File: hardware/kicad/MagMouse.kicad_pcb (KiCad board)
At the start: 4 copper layers, 50 x 95 mm, 316 parts, among them J1 TYPE-C-31-M-12, J2 COIL_L, J3 COIL_M, J4 COIL_R, J5 GB1806 phase wires, Q1 2N7002, Q2 2N7002, Q3 2N7002, Q4 2N7002, Q5 AO3400A, SW1 RESET, SW2 BOOT, U1 TPD2EUSB30DRTR, U10 ADS7038IRTER, U11 TUSB320LAIRWBR, U12 TPS259470LRPWR, U13 TPS259470LRPWR, U14 SN74LVC2G04DCKR, U15 SN74LVC1G123DCUR, U16 SN74LVC08APWR, U17 SN74LVC08APWR, U18 SN74LVC08APWR, U19 TLV9001IDBVR, U2 TPS62162DSGR, U20 TPD2E2U06DCKR, U21 DRV8316RRGFR, U22 SN74LVC08APWR, U23 ADS7038IRTER, U24 SN74LVC125APWR, U25 SN74LVC125APWR, U26 SN74LVC125APWR, U27 MA735GGU-P, U28 TPS22919DCKR, U29 SN74LVC125APWR, U3 ESP32-S3-MINI-1-N8, U30 TLV1811DBVR, U31 LM4040AIM3-2.5/NOPB, U32 ICM-42688-P, U33 TPS7A2450DBVR, U34 SN74LV1T34DBVR, U35 PMW3360DM-T2QU, U36 TLV75519PDBVR, U37 SN74LVC125APWR, U38 TPS22918DBVR, U39 SN74LVC1G125DBVR, U4 DRV8231ADSGR, U5 DRV8231ADSGR, U6 DRV8231ADSGR, U7 TMAG5253BA2IQDMRR, U8 TMAG5253BA2IQDMRR, U9 TMAG5253BA2IQDMRR

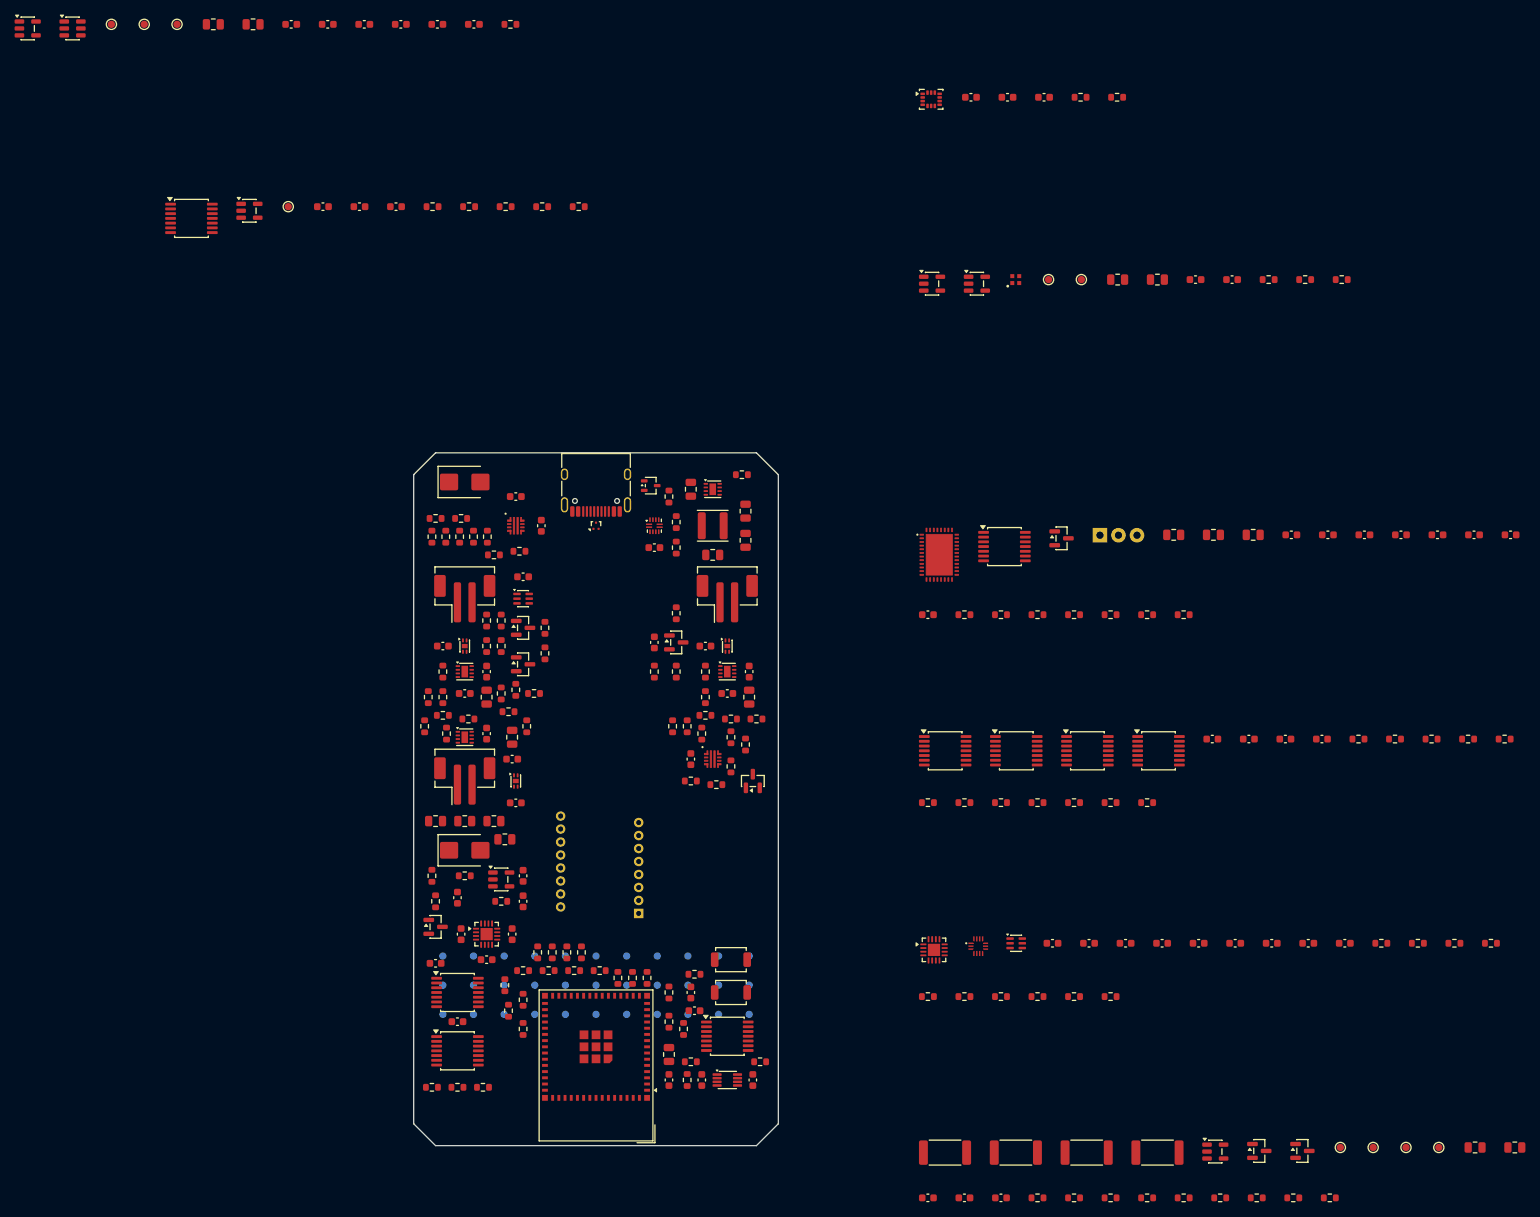
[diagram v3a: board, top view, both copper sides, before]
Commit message: Place motherboard, add upright encoder PCB and route logic buck
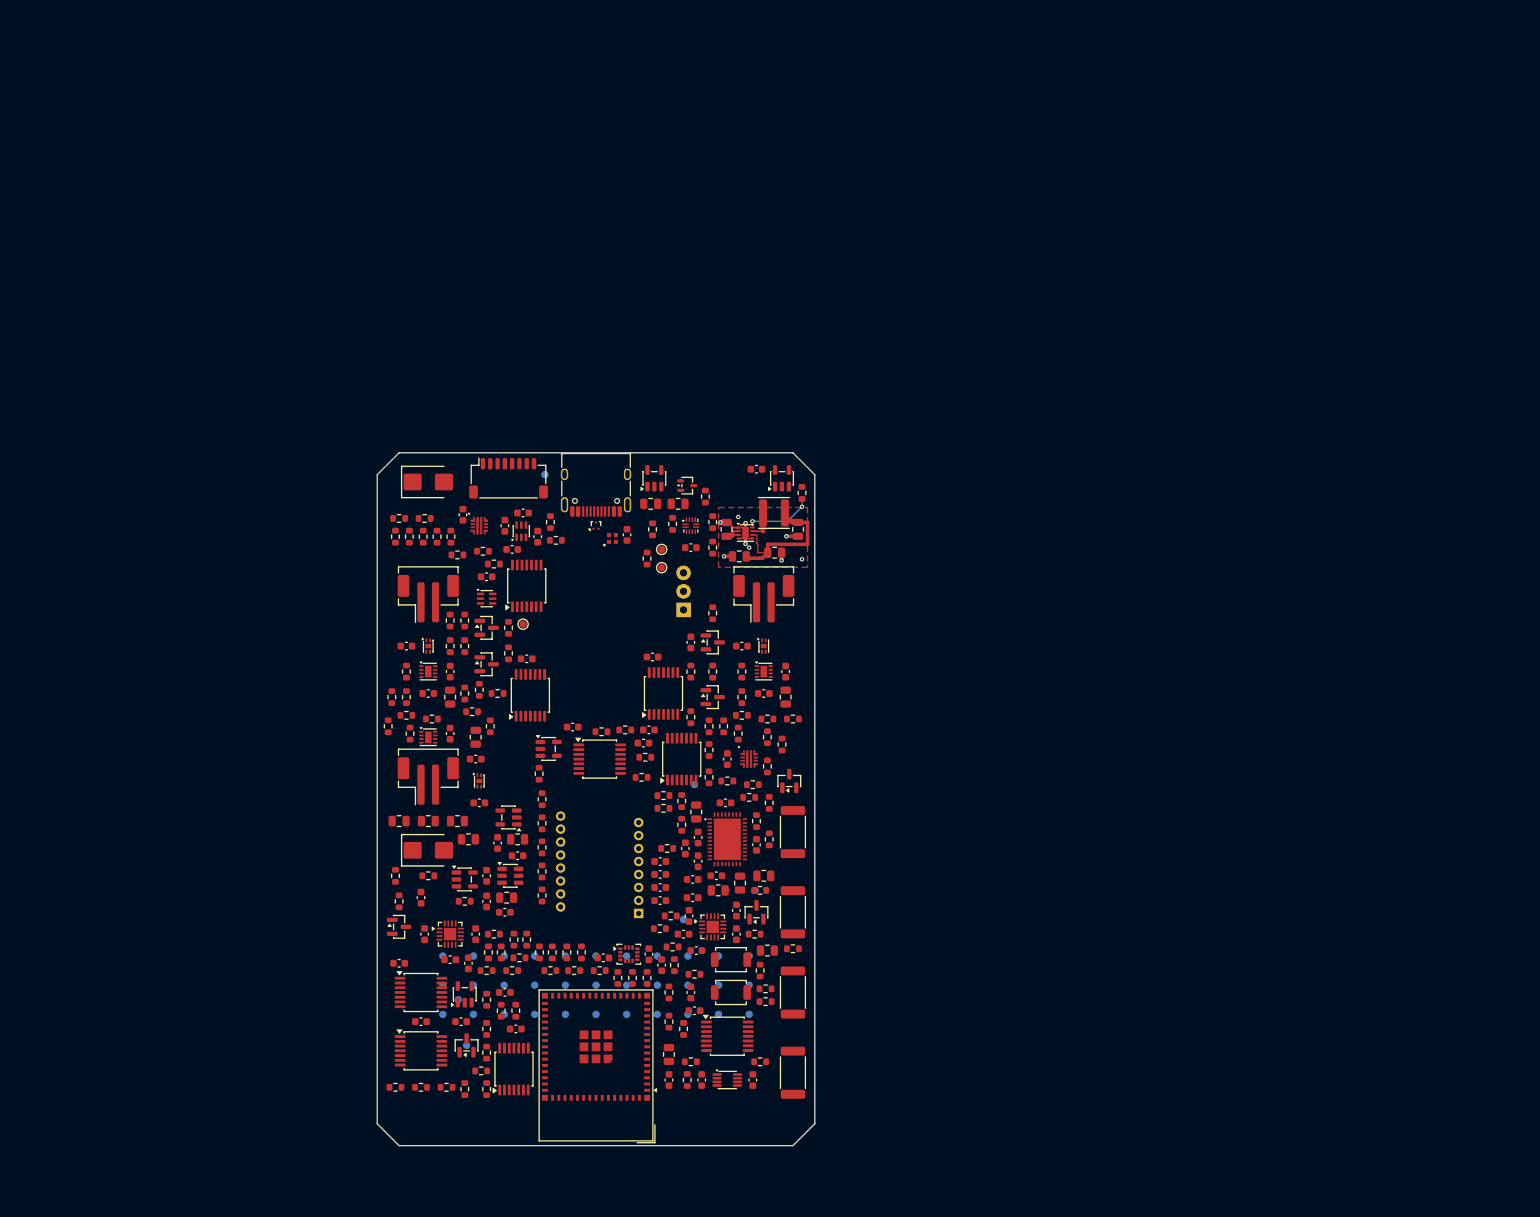
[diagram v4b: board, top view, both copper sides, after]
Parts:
- removed C62: 1uF/50V, Capacitor_SMD:C_0603_1608Metric
- removed U27: MA735GGU-P, MagMouse:MPS_UTQFN14_2x2
- added J6: ENCODER_8P, Connector_JST:JST_SH_SM08B-SRSS-TB_1x08-1MP_P1.00mm_Horizontal, F.Cu at (113.0, 103.5)
- TP34, TP35, TP36, TP40, TP41, TP42, TP43: moved to B.Cu
- moved TP40 148.0 mm to (146.8, 160.0), turned to 180 degrees
- moved TP37 144.6 mm to (115.0, 123.5)
- moved TP41 143.0 mm to (142.8, 160.0), turned to 180 degrees
- moved TP34 142.8 mm to (118.0, 103.0), turned to 180 degrees
- moved R127 142.7 mm to (118.8, 171.0)
- moved TP42 141.0 mm to (137.0, 164.0), turned to 180 degrees
- moved C72 132.6 mm to (126.0, 169.2)
- moved TP36 131.5 mm to (106.1, 175.0)
- moved R126 131.4 mm to (135.8, 170.2), turned to 90 degrees
- moved U38 130.8 mm to (113.2, 158.0)
- moved C71 128.1 mm to (134.0, 170.2), turned to 90 degrees
- moved C64 127.2 mm to (115.0, 108.2)
- moved U36 126.7 mm to (113.0, 150.0), turned to 180 degrees
- moved C77 126.3 mm to (112.8, 161.0)
- moved C70 125.5 mm to (132.2, 168.8), turned to 90 degrees
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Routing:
- net +3V3: track 0.00 -> 21.5 mm
- net GND: track 0.00 -> 10.7 mm, vias 0 -> 9
- net LOGIC_PG: track 0.00 -> 9.55 mm, vias 0 -> 2
- net BUCK_SW: track 0.00 -> 3.95 mm
- net PWR_5V: track 0.00 -> 3.65 mm
- added copper zone on F.Cu, net GND
- added copper zone on In1.Cu, net GND
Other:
- board size 50 x 95 mm -> 60 x 95 mm
- board text added: "60 x 95 mm - PROVISIONAL OUTLINE"
- board text added: "J6 -> ENCODER J7 / PIN N TO PIN N VERIFY PLUG + WIRE CLEARANCE ABOVE FRONT PARTS"
- board text added: "WHEEL + UPRIGHT ENCODER - PROVISIONAL"
- board text removed: "50 x 95 mm - PROVISIONAL OUTLINE"
- board text removed: "IMU"
- board text removed: "RGB"
- board text removed: "STAGED 10 Wheel Driver - NOT PLACED"
- board text removed: "STAGED 11 Wheel SPI - NOT PLACED"
- board text removed: "STAGED 12 Wheel Feedback - NOT PLACED"
- board text removed: "STAGED 13 Regeneration Brake - NOT PLACED"
- board text removed: "STAGED 14 IMU - NOT PLACED"
- board text removed: "STAGED 15 RGB Status - NOT PLACED"
- board text removed: "STAGED 16 Optical Power - NOT PLACED"
- board text removed: "STAGED 17 Optical Support - U35 ON BOARD"
- board text removed: "WHEEL DRIVE / ADC2 BRAKE RESERVE"
- board text removed: "WHEEL MECHANICS PROVISIONAL"

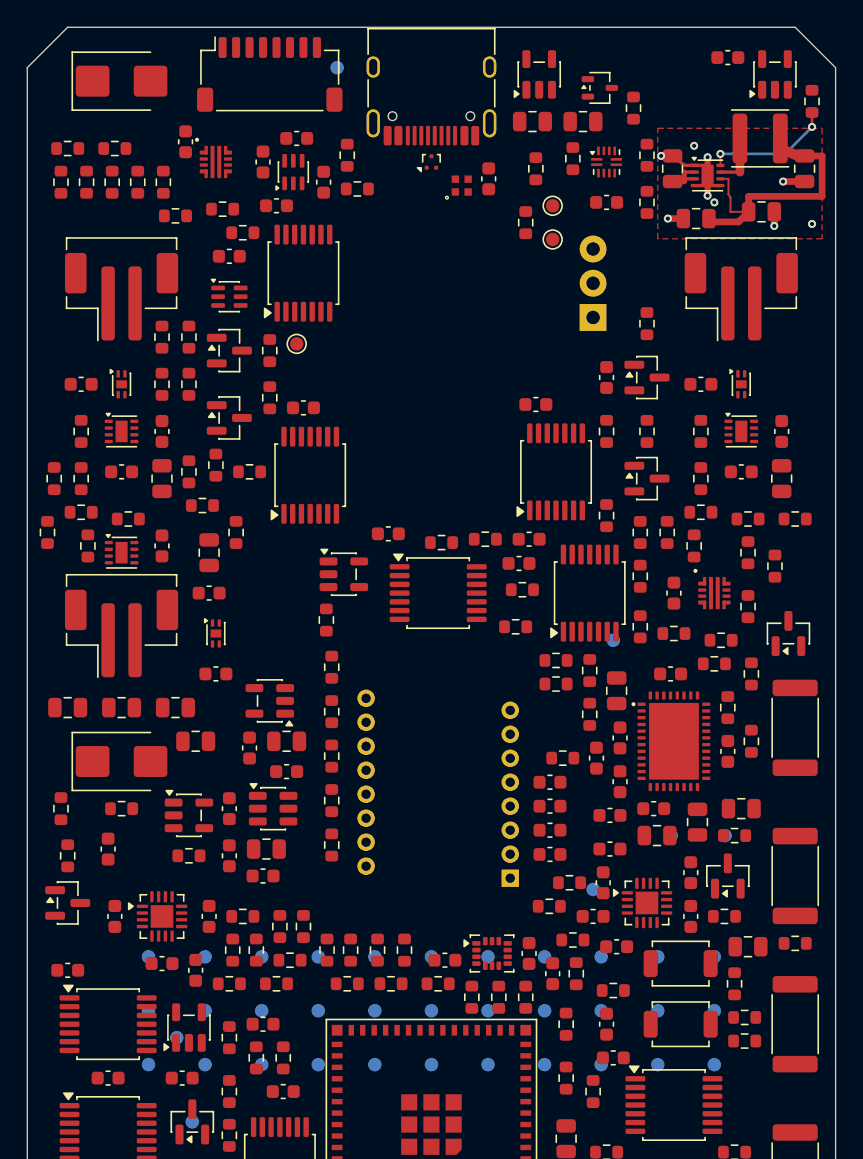
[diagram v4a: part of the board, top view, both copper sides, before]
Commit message: Route input power and Type-C detection, select PCB stackup
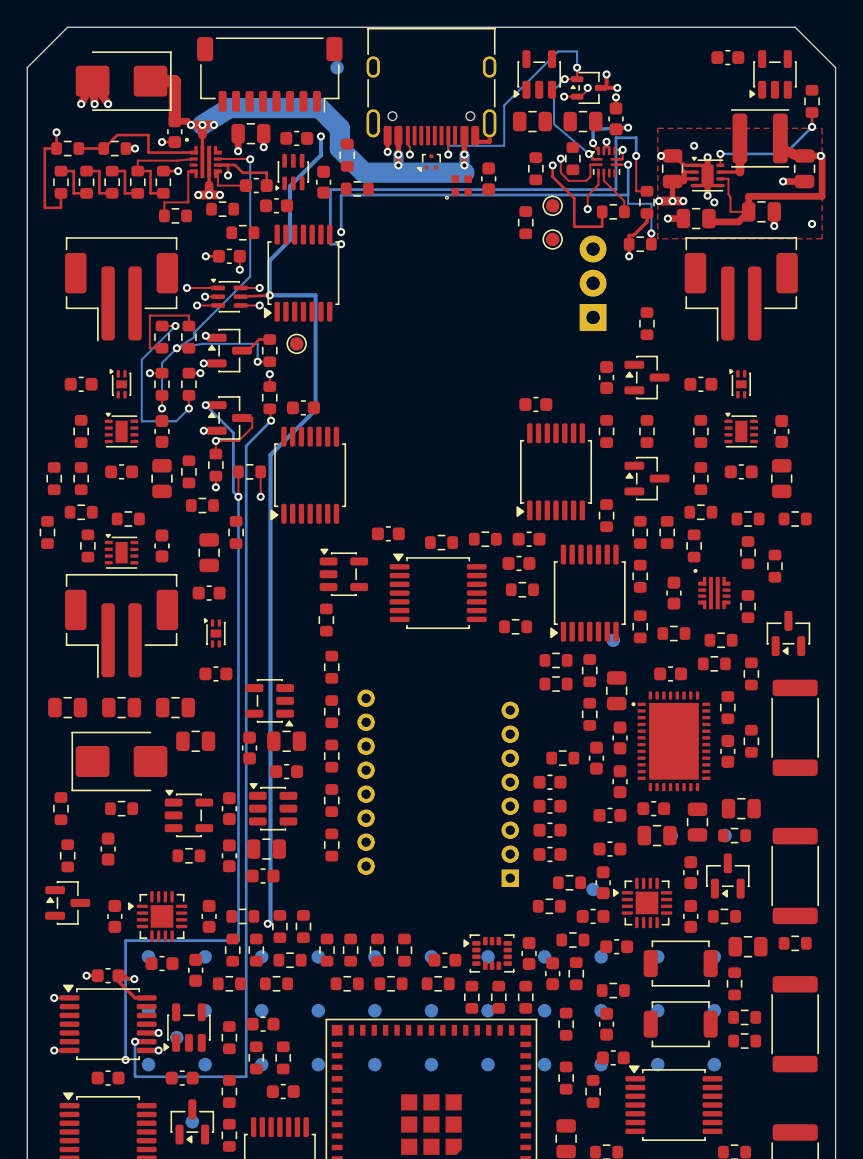
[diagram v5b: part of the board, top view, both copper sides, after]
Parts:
- added C88: 10uF/25V, Capacitor_SMD:C_0805_2012Metric, F.Cu at (111.6, 107.9)
- moved R25 7.84 mm to (138.5, 113.7), turned to 0 degrees
- moved R26 6.62 mm to (140.5, 116.1), turned to 0 degrees
- moved C22 6.24 mm to (138.7, 106.8), turned to 90 degrees
- moved C29 3.03 mm to (101.0, 170.4), turned to 180 degrees
- moved C25 1.82 mm to (112.0, 111.8), turned to 0 degrees
- moved C24 1.10 mm to (106.0, 107.8), turned to -90 degrees
- moved U20 0.80 mm to (136.7, 104.5)
- moved U12 0.75 mm to (108.2, 110.0)
- turned D1 to 180 degrees
- turned J6 to 180 degrees
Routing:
- net +3V3: track 21.5 -> 211.4 mm, vias 0 -> 9
- net SOURCE_OK: track 0.00 -> 90.1 mm, vias 0 -> 5
- net VBUS_USB: track 0.00 -> 73.9 mm, vias 0 -> 9
- net SOURCE_3A: track 0.00 -> 64.7 mm, vias 0 -> 4
- net CC_OUT2_INV: track 0.00 -> 61.5 mm, vias 0 -> 2
- net CC_OUT2: track 0.00 -> 55.4 mm, vias 0 -> 4
- net USB_ILM: track 0.00 -> 54.1 mm, vias 0 -> 5
- net PWR_5V: track 3.65 -> 54.8 mm, vias 0 -> 7
- net CC_OUT1: track 0.00 -> 50.5 mm, vias 0 -> 4
- net GND: track 10.7 -> 47.4 mm, vias 9 -> 32
- net USB_CC2: track 0.00 -> 29.0 mm, vias 0 -> 4
- net USB_CC1: track 0.00 -> 27.1 mm, vias 0 -> 4
- net ILM_HIGH_D: track 0.00 -> 15.1 mm, vias 0 -> 2
- net ILM_BASE_2: track 0.00 -> 14.0 mm, vias 0 -> 2
- net USB_UVLO: track 0.00 -> 10.2 mm
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
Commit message: Route U13 local actuator power and protection
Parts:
- added C89: 1uF/50V, Capacitor_SMD:C_0603_1608Metric, F.Cu at (146.0, 139.0)
- moved C40 38.6 mm to (145.2, 144.9)
- moved R42 10.6 mm to (151.0, 138.1)
- moved C26 6.39 mm to (148.5, 145.2), turned to 0 degrees
- moved R43 5.46 mm to (151.0, 142.4)
- moved R40 3.16 mm to (153.5, 139.0)
- moved D3 0.32 mm to (151.8, 145.1)
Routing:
- net PWR_5V: track 54.8 -> 104.3 mm, vias 7 -> 12
- net ACT_UVLO: track 0.00 -> 30.3 mm, vias 0 -> 3
- net ACT_OVLO: track 0.00 -> 19.6 mm, vias 0 -> 3
- net ACT_ILM: track 0.00 -> 9.05 mm
- net GND: track 47.4 -> 54.6 mm, vias 32 -> 39
- net ACT_5V: track 0.00 -> 6.95 mm, vias 0 -> 3
- net ACT_UV_2: track 0.00 -> 4.65 mm
- net ACT_UV_1: track 0.00 -> 3.65 mm
- net ACT_DVDT: track 0.00 -> 3.02 mm

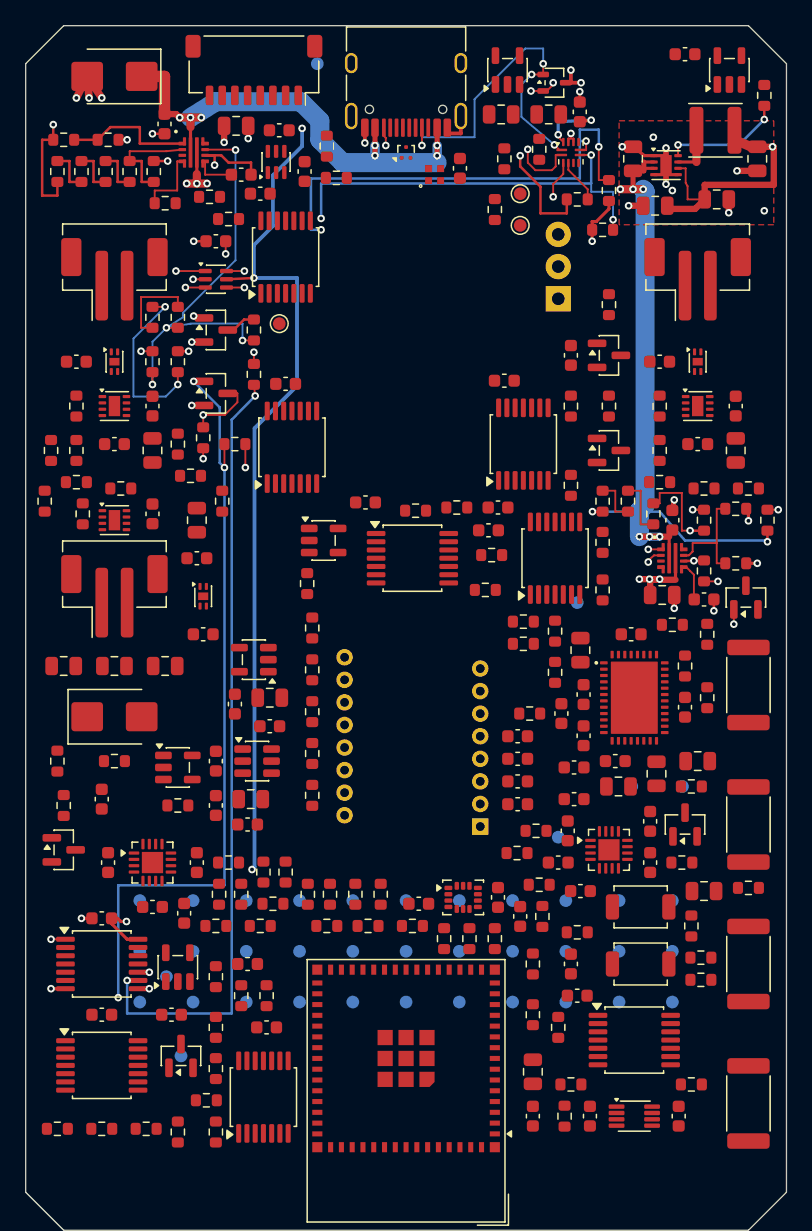
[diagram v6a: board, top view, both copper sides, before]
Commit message: Route actuator distribution and USB data with copper validation
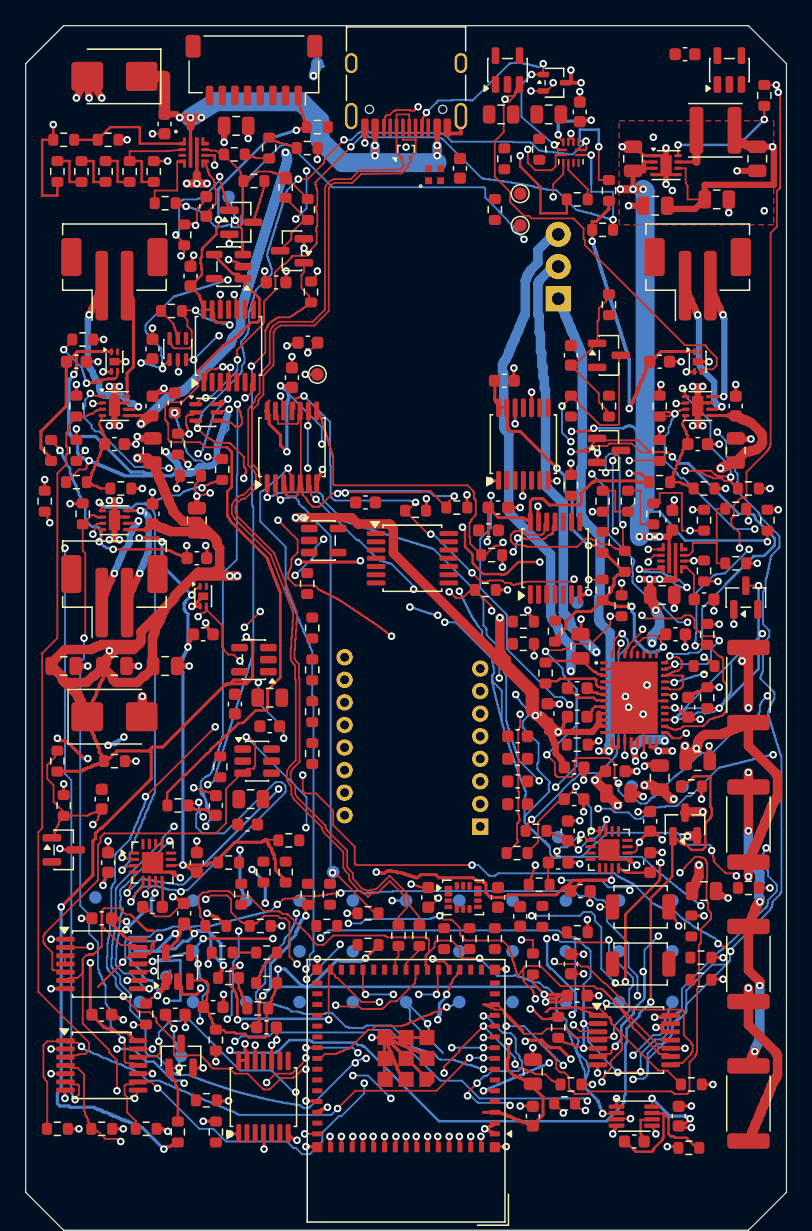
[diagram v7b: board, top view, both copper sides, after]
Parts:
- moved TP14 59.5 mm to (111.0, 113.5)
- moved R45 45.8 mm to (142.0, 145.8), turned to 90 degrees
- moved R119 43.9 mm to (104.5, 177.9), turned to -90 degrees
- moved U19 39.7 mm to (111.0, 119.0), turned to 180 degrees
- moved C34 38.0 mm to (114.8, 120.2), turned to 0 degrees
- moved R110 24.6 mm to (99.5, 124.8), turned to 0 degrees
- moved R61 19.8 mm to (117.2, 114.5), turned to -90 degrees
- moved R58 19.7 mm to (117.2, 109.7), turned to 0 degrees
- moved C63 18.4 mm to (105.0, 125.5)
- moved R70 18.4 mm to (137.5, 185.0), turned to 180 degrees
- moved R60 17.3 mm to (115.5, 112.8), turned to -90 degrees
- moved R49 17.0 mm to (137.0, 179.0), turned to 90 degrees
- moved U28 16.7 mm to (107.0, 125.5)
- moved R57 16.2 mm to (114.2, 109.7)
- moved R7 15.8 mm to (115.8, 164.2), turned to 0 degrees
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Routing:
- net ACT_5V: track 6.95 -> 499.2 mm, vias 3 -> 34
- net +3V3: track 211.4 -> 581.8 mm, vias 9 -> 50
- net MCU_EN: track 0.00 -> 258.4 mm, vias 0 -> 12
- net ACT_DRIVE_EN: track 0.00 -> 239.3 mm, vias 0 -> 22
- net GND: track 54.6 -> 293.4 mm, vias 39 -> 214
- net HALL_EN: track 0.00 -> 219.3 mm, vias 0 -> 12
- net DRV_FAULT_N: track 0.00 -> 218.9 mm, vias 0 -> 16
- net BTN_R_IN2: track 0.00 -> 165.7 mm, vias 0 -> 10
- net BTN_R_IN1: track 0.00 -> 163.9 mm, vias 0 -> 9
- net DRV_AVDD: track 0.00 -> 138.7 mm, vias 0 -> 14
- net BTN_R_ISENSE: track 0.00 -> 134.4 mm, vias 0 -> 7
- net WHEEL_RUN_EN: track 0.00 -> 126.3 mm, vias 0 -> 6
- net ACT_FAULT_N: track 0.00 -> 124.3 mm, vias 0 -> 10
- net WHEEL_PWM_C: track 0.00 -> 118.8 mm, vias 0 -> 12
- net VBUS_PRESENT_N: track 0.00 -> 118.2 mm, vias 0 -> 8
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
